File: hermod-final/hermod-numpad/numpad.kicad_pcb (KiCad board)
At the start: 2 copper layers, 77.4 x 99.3 mm, 46 parts

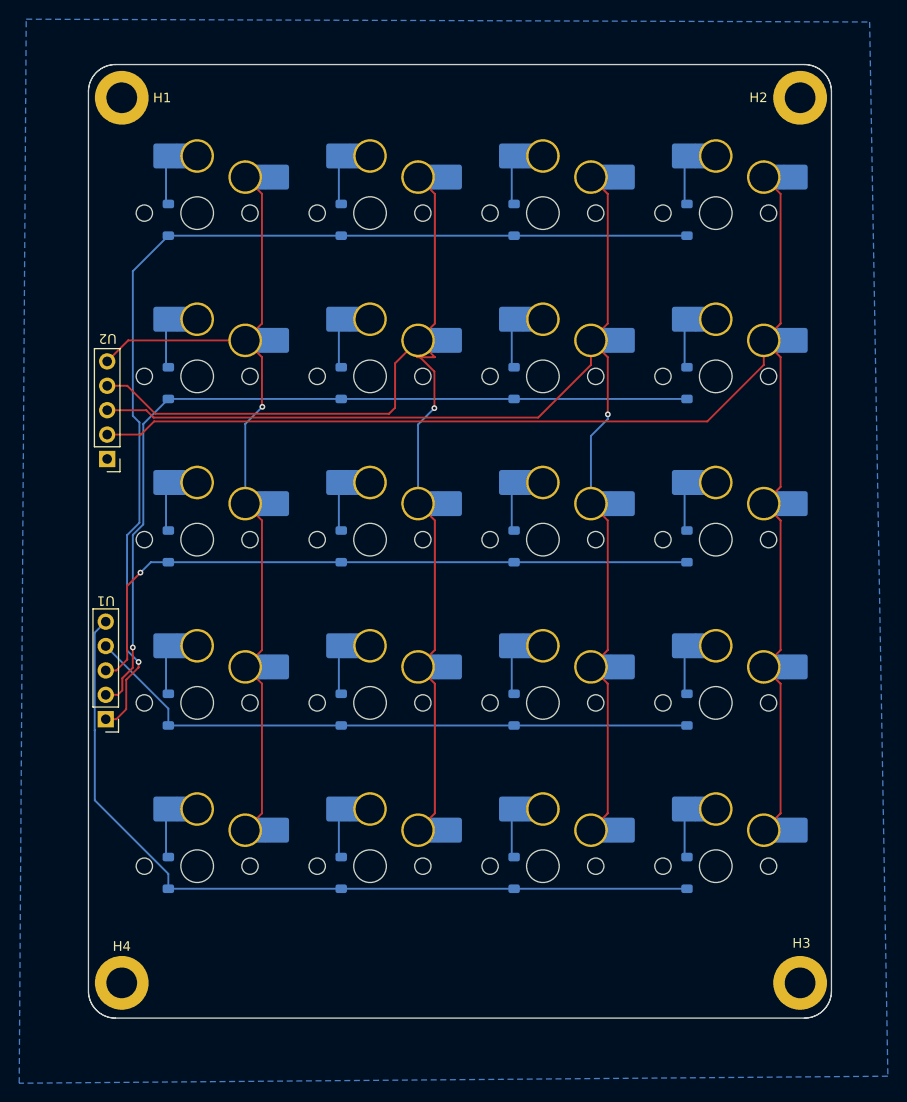
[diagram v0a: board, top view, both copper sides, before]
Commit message: Fixed random trace on numpad
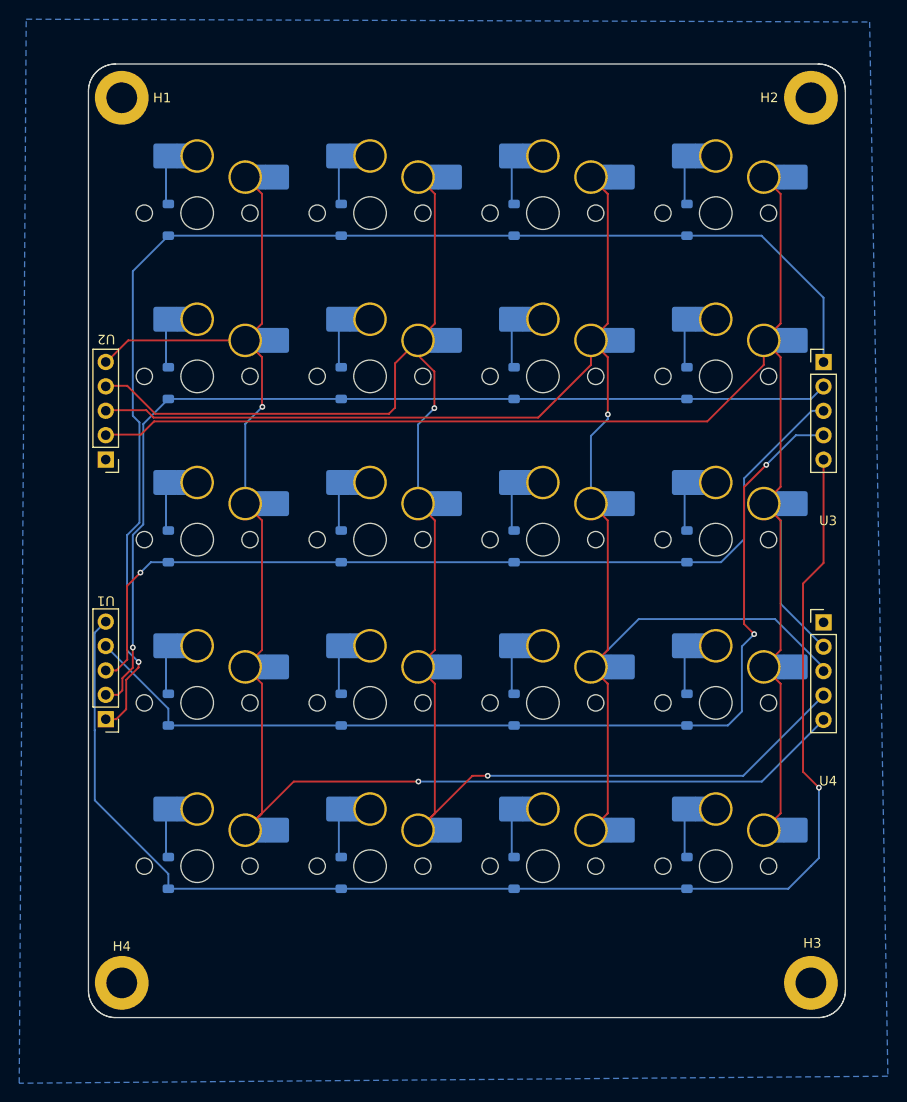
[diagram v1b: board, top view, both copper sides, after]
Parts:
- added U3: ~, Pogo:Pogo_2.54mm_5p, F.Cu at (101.2, 54.6)
- added U4: ~, Pogo:Pogo_2.54mm_5p, F.Cu at (101.2, 81.7)
- moved H2 1.13 mm to (99.9, 22.0)
- moved H3 1.13 mm to (99.9, 114.2)
- moved U2 0.16 mm to (26.5, 54.5)
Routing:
- net col7: track 89.1 -> 154.1 mm, vias 1 -> 2
- net row4: track 85.5 -> 143.6 mm, vias 0 -> 1
- net col8: track 116.0 -> 159.4 mm, vias 1 -> 2
- net row3: track 65.0 -> 106.1 mm, vias 0 -> 2
- net col9: track 129.3 -> 158.1 mm
- net row2: track 69.7 -> 94.2 mm
- net row0: track 109.3 -> 132.9 mm
- net col10: track 147.7 -> 165.2 mm
- net row1: track 88.2 -> 103.0 mm
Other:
- board size 77.4 x 99.3 mm -> 78.8 x 99.3 mm

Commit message: Updated logos on the boards
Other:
- board text added: "Designed By: Charlie Steenhagen Modern Hobbyist"
